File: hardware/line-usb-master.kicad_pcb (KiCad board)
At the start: 2 copper layers, 79.5 x 50 mm, 109 parts, among them J1 USB_B, J2 Conn_01x02, J3 Banana, J4 Conn_01x01, J5 Conn_01x01, J6 Conn_01x01, Q6 2N7002, SW1 SW_SPDT, SW2 SW_SPDT, SW3 SW_SPDT, SW4 TVCM17015BPB, U1 TPS61085, U3 FT4232H, U4 MCP2003, U5 93LCxxC, U6 MCP2003, U7 74HCT595, U8 LMR51420, Y1 CFPX-104

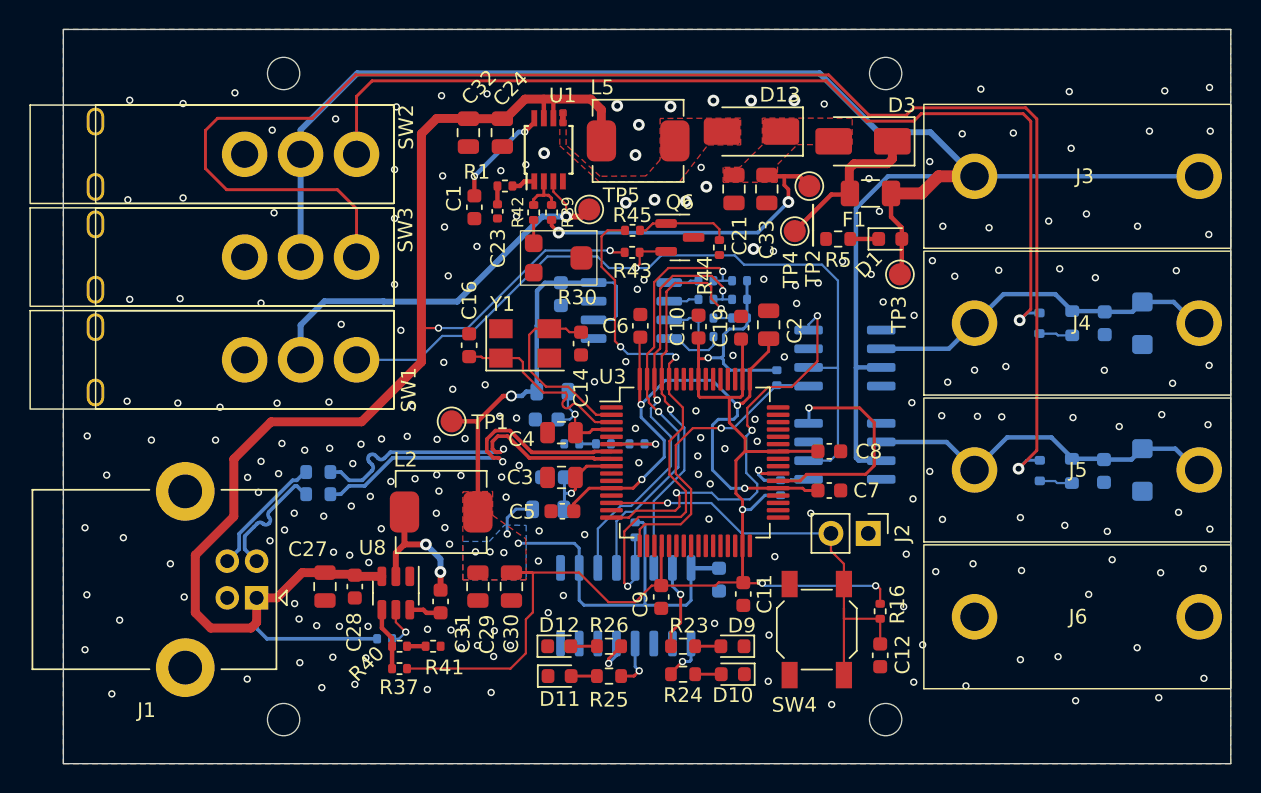
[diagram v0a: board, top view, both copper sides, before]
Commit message: Hardware fixes
Crystal 4th pin connected to GND
Removed series resistor from USB lines
Corrected pullup on EEPROM lines
Fixes PWREN Mosfet orientation
Added fiducial
Added 4 pin connectors for direct wired variant
Increased pad size of the front panel switches
Added 3d model to shift register
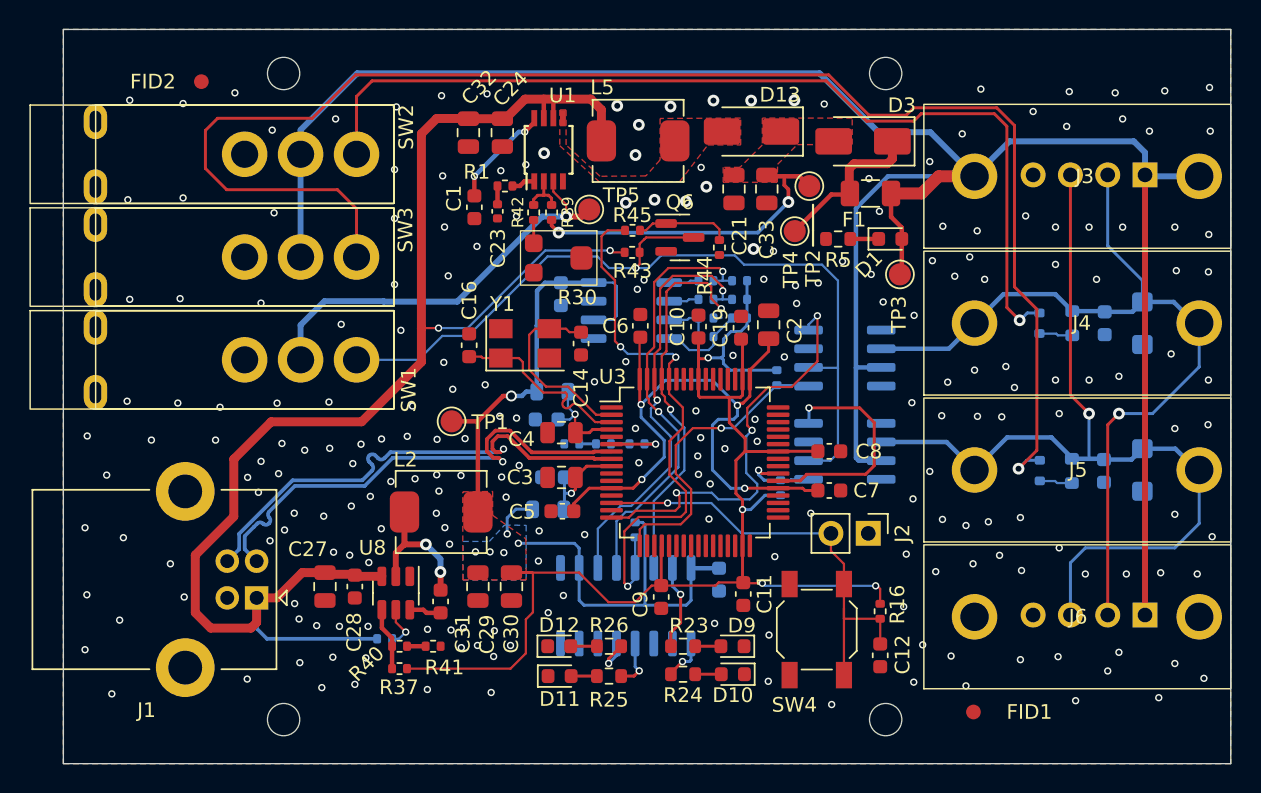
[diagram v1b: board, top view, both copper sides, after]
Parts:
- removed R11, R12: 22, Resistor_SMD:R_0603_1608Metric
- added FID1: Fiducial, Fiducial:Fiducial_1mm_Mask2mm, F.Cu at (162.0, 116.5)
- added FID2: Fiducial, Fiducial:Fiducial_1mm_Mask2mm, F.Cu at (109.4, 73.6)
- added J7: Conn_01x04, Connector_PinHeader_2.54mm:PinHeader_1x04_P2.54mm_Vertical, B.Cu at (173.7, 109.9)
- added J8: Conn_01x04, Connector_PinHeader_2.54mm:PinHeader_1x04_P2.54mm_Vertical, B.Cu at (173.7, 79.9)
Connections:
- Q6 pad 2: /PWREN -> GND
- Q6 pad 3: GND -> /PWREN
- R17 pad 2: /EEDATA -> Net-(U5-DO)
- U3 pad 7: /USB- -> /USB_N
- U3 pad 8: /USB+ -> /USB_P
- Y1 pad 4: unconnected-(Y1-Pad4) -> GND
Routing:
- net Net-(D8-A2): track 24.6 -> 61.6 mm, vias 0 -> 1
- net Net-(D7-A2): track 24.2 -> 57.6 mm, vias 0 -> 1
- net +BATT: track 115.7 -> 148.6 mm
- net /USB_N: track 8.46 -> 34.1 mm, vias 0 -> 1
- net /USB_P: track 8.51 -> 34.1 mm, vias 0 -> 1
- net /USB-: track 24.4 -> 0.00 mm, vias 1 -> 0
- net /USB+: track 24.4 -> 0.00 mm, vias 1 -> 0
- net /PWREN: track 56.0 -> 58.7 mm
- net Net-(U5-DO): track 3.49 -> 5.28 mm
- net Net-(D5-A): track 67.3 -> 65.5 mm
- net Net-(D6-A): track 103.2 -> 102.0 mm
- net /EEDATA: track 27.5 -> 26.8 mm
- net GND: vias 220 -> 233
